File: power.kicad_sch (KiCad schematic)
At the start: 33 parts, among them U300 TPS563200, U301 TPS563200

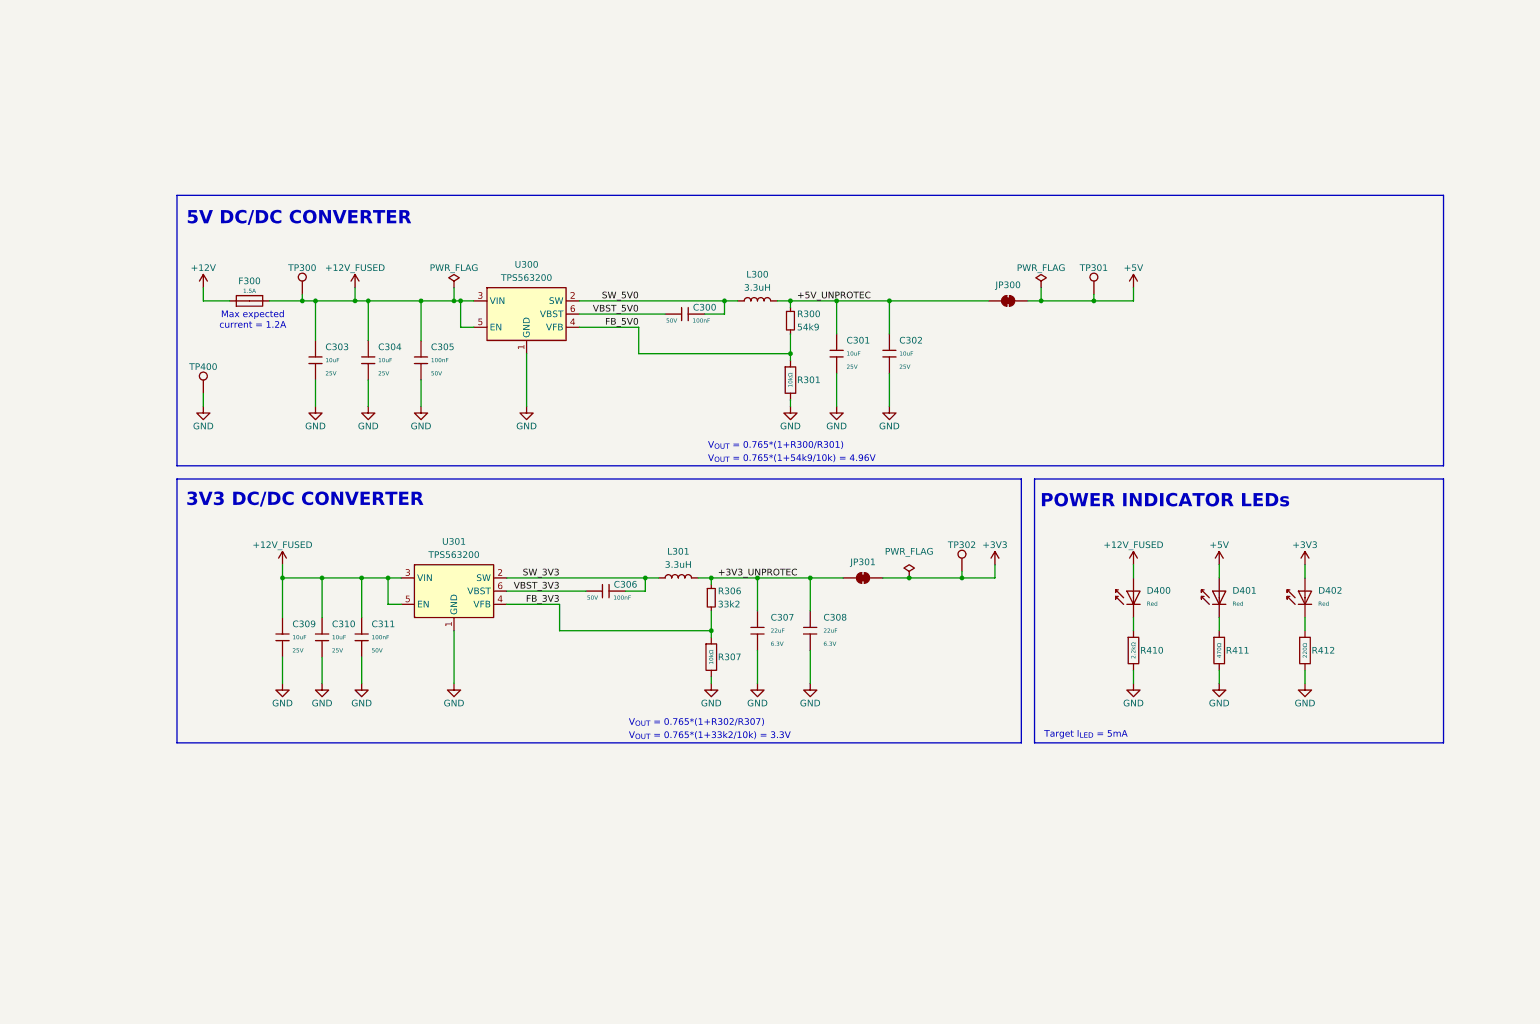
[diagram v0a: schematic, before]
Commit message: Add MX74700 lib and symbol
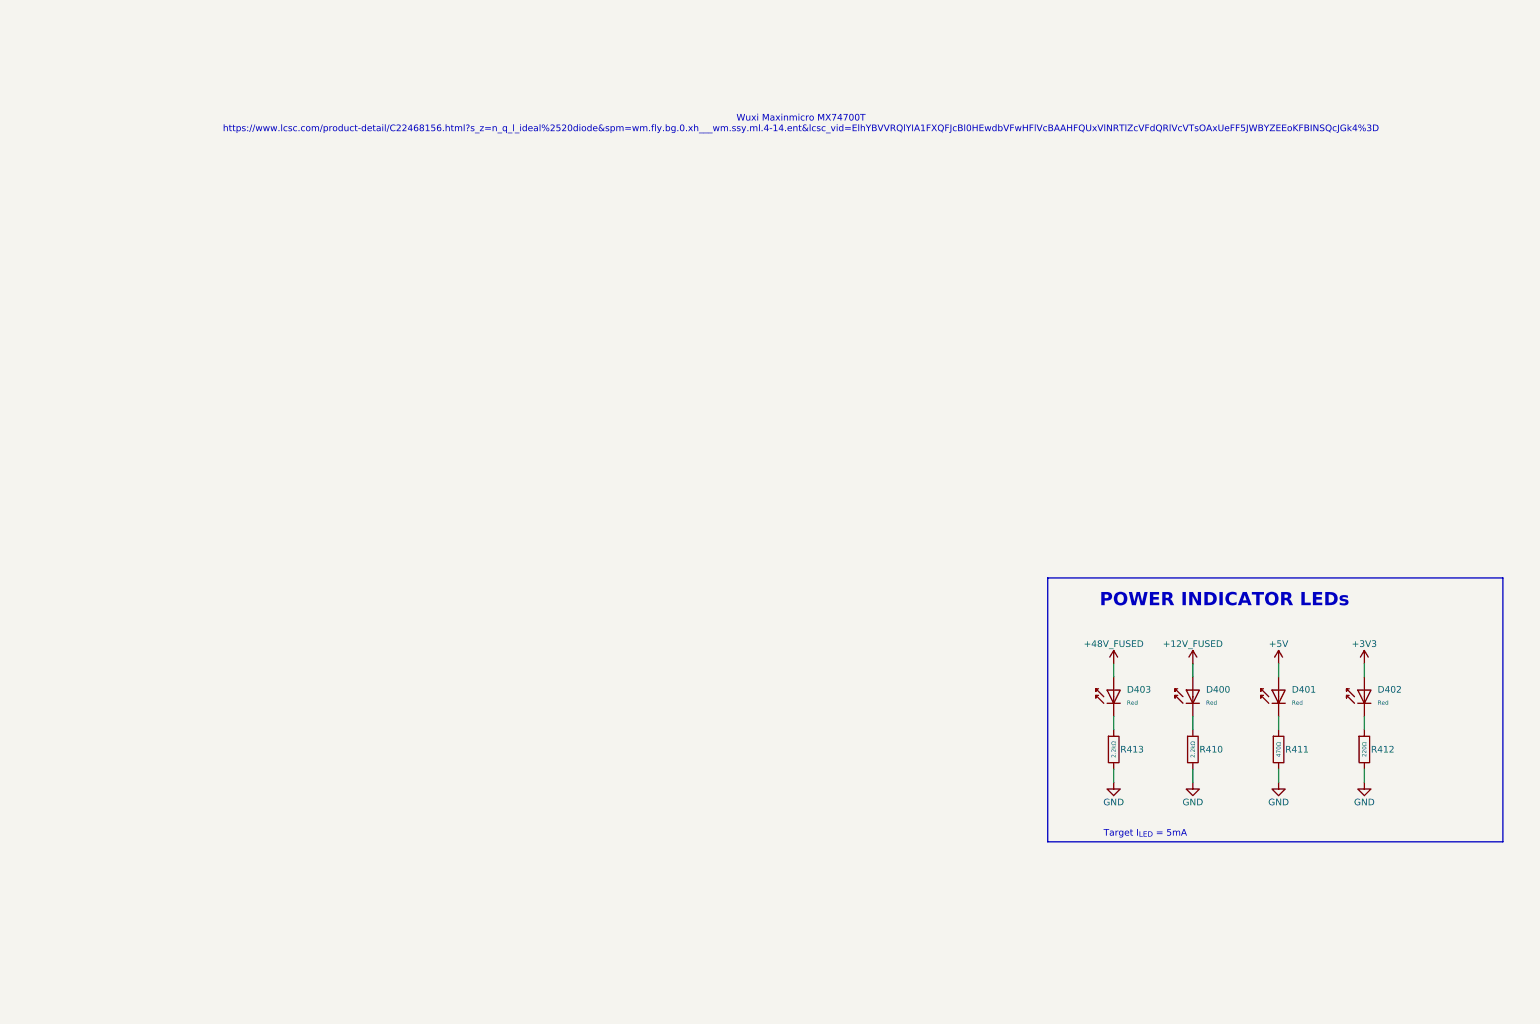
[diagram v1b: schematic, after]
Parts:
- removed C300, C305, C306, C311: 100nF, PCM_JLCPCB:C_0402, symbol PCM_JLCPCB-Capacitors:0402,100nF,(2)
- removed C301, C302, C303, C304, C309, C310: 10uF, PCM_JLCPCB:C_0603, symbol PCM_JLCPCB-Capacitors:0603,10uF,(2)
- removed C307, C308: 22uF, PCM_JLCPCB:C_0603, symbol PCM_JLCPCB-Capacitors:0603,22uF
- removed F300: 1.5A, PCM_JLCPCB:F_0603, symbol PCM_JLCPCB-Variable-Resistors:Fuse,1.5A
- removed JP300, JP301: SolderJumper_2_Bridged, Jumper:SolderJumper-2_P1.3mm_Open_TrianglePad1.0x1.5mm, symbol Jumper:SolderJumper_2_Bridged
- removed L300, L301: 3.3uH, Inductor_SMD:L_Changjiang_FXL0420, symbol Device:L
- removed R300: 54k9, PCM_JLCPCB:R_0402, symbol Device:R_Small
- removed R301, R307: 10kΩ, PCM_JLCPCB:R_0402, symbol PCM_JLCPCB-Resistors:0402,10kΩ
- removed R306: 33k2, PCM_JLCPCB:R_0402, symbol Device:R_Small
- removed TP300, TP301, TP302, TP400: TestPoint, TestPoint:TestPoint_Pad_D1.0mm, symbol Connector:TestPoint
- removed U300, U301: TPS563200, Package_TO_SOT_SMD:SOT-23-6, symbol Regulator_Switching:TPS563200
- added D403: Red, PCM_JLCPCB:D_0603, symbol PCM_JLCPCB-Diodes:LED,0603,Red
- added R413: 2.2kΩ, PCM_JLCPCB:R_0402, symbol PCM_JLCPCB-Resistors:0402,2.2kΩ
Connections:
- net GND: now also R413.2
- new net: D403.1, R413.1
- new net +48V_FUSED: D403.2
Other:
- note added: "Wuxi Maxinmicro MX74700T https://www.lcsc.com/product-detail/C22468156.html?s_z=n_q_l_ideal%2520diode&spm=wm.fly.bg.0.xh___wm.ssy.ml.4-14.ent&lcsc_vid=ElhYBVVRQlYIA1FXQFJcBl0HEwdbVFwHFlVcBAAHFQUxVlNRTlZcVFdQRlVcVTsOAxUeFF5JWBYZEEoKFBINSQcJGk4%3D"
- note removed: "3V3 DC/DC CONVERTER"
- note removed: "5V DC/DC CONVERTER"
- note removed: "Max expected current = 1.2A"
- note removed: "V_{OUT} = 0.765*(1+33k2/10k) = 3.3V"
- note removed: "V_{OUT} = 0.765*(1+54k9/10k) = 4.96V"
- note removed: "V_{OUT} = 0.765*(1+R300/R301)"
- note removed: "V_{OUT} = 0.765*(1+R302/R307)"
- title: ModuCard BM STM32H562VGT6 -> ModuCard 3 BM STM32H562VGT6
- moved on the sheet: D400, D401, D402, R410, R411, R412

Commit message: Write converter schematics
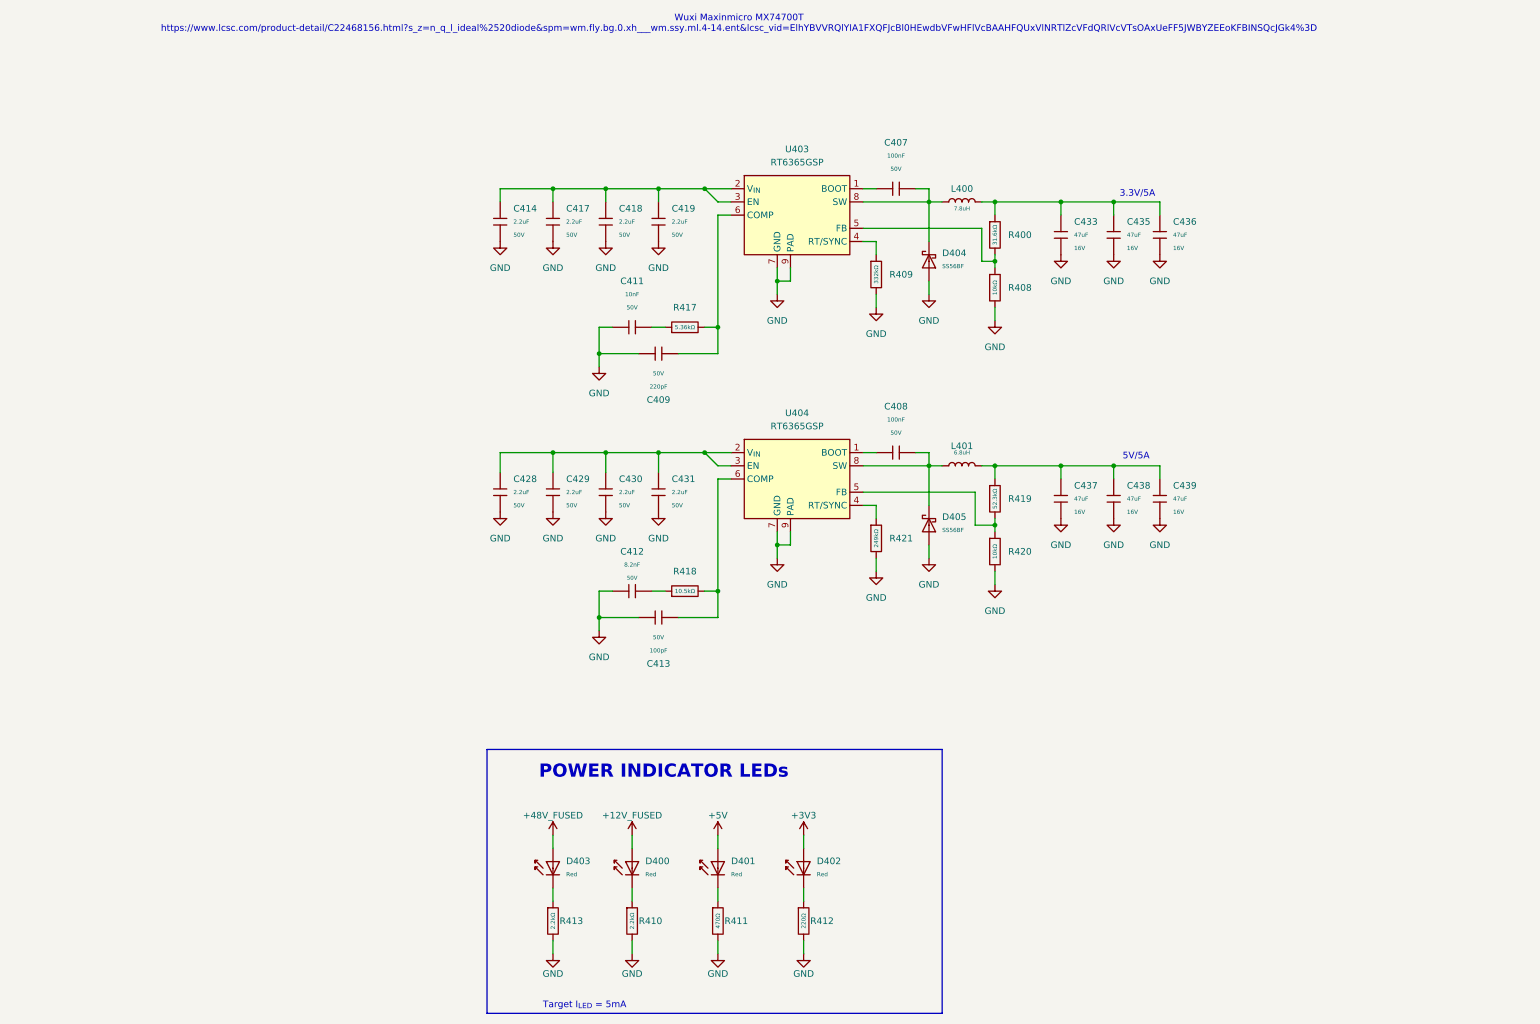
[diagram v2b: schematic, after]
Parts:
- added C407, C408: 100nF, PCM_JLCPCB:C_0603, symbol PCM_JLCPCB-Capacitors:0603,100nF
- added C409: 220pF, PCM_JLCPCB:C_0402, symbol PCM_JLCPCB-Capacitors:0402,220pF
- added C411: 10nF, PCM_JLCPCB:C_0402, symbol PCM_JLCPCB-Capacitors:0402,10nF
- added C412: 8.2nF, PCM_JLCPCB:C_0402, symbol PCM_JLCPCB-Capacitors:0402,10nF
- added C413: 100pF, PCM_JLCPCB:C_0402, symbol PCM_JLCPCB-Capacitors:0402,100pF
- added C414, C417, C418, C419, C428, C429, C430, C431: 2.2uF, PCM_JLCPCB:C_1206, symbol PCM_JLCPCB-Capacitors:1206,2.2uF
- added C433, C435, C436, C437, C438, C439: 47uF, Capacitor_SMD:C_1210_3225Metric, symbol PCM_JLCPCB-Capacitors:0603,100nF
- added D404, D405: SS56BF, PCM_JLCPCB:D_SMBF, symbol PCM_JLCPCB-Diodes:Schottky,SS56BF
- added L400: 7.8uH, Inductor_SMD:L_APV_APH1050, symbol FHC1050:FHC1050-7R8M
- added L401: 6.8uH, Inductor_SMD:L_Sunlord_MWSA0605S, symbol PSPMAA0605H:PSMAA0605H-6R8M-ANP
- added R400: 31.6kΩ, PCM_JLCPCB:R_0402, symbol PCM_JLCPCB-Resistors:0402,33kΩ
- added R408, R420: 10kΩ, PCM_JLCPCB:R_0402, symbol PCM_JLCPCB-Resistors:0402,10kΩ
- added R409: 332kΩ, PCM_JLCPCB:R_0402, symbol PCM_JLCPCB-Resistors:0402,0Ω
- added R417: 5.36kΩ, PCM_JLCPCB:R_0402, symbol PCM_JLCPCB-Resistors:0402,0Ω
- added R418: 10.5kΩ, PCM_JLCPCB:R_0402, symbol PCM_JLCPCB-Resistors:0402,0Ω
- added R419: 52.3kΩ, PCM_JLCPCB:R_0402, symbol PCM_JLCPCB-Resistors:0402,33kΩ
- added R421: 249kΩ, PCM_JLCPCB:R_0402, symbol PCM_JLCPCB-Resistors:0402,0Ω
- added U403, U404: RT6365GSP, Package_SO:SOIC-8-1EP_3.9x4.9mm_P1.27mm_EP2.29x3mm, symbol RT6365:RT6365GSP
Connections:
- net GND: now also C409.1, C411.1, C412.1, C413.1, C414.2, C417.2, C418.2, C419.2, C428.2, C429.2, C430.2, C431.2, C433.2, C435.2, C436.2, C437.2, C438.2, C439.2, D404.2, D405.2, R408.2, R409.2, R420.2, R421.2, U403.7 (GND), U403.9 (PAD), U404.7 (GND), U404.9 (PAD)
- new net: C414.1, C417.1, C418.1, C419.1, U403.2 (V_{IN}), U403.3 (EN)
- new net: R400.2, R408.1, U403.5 (FB)
- new net: C407.2, D404.1, L400.1, U403.8 (SW)
- new net: C408.2, D405.1, L401.1, U404.8 (SW)
- new net: C437.1, C438.1, C439.1, L401.2, R419.1
- new net: C433.1, C435.1, C436.1, L400.2, R400.1
- new net: C407.1, U403.1 (BOOT)
- new net: R409.1, U403.4 (RT/SYNC)
- new net: C409.2, R417.2, U403.6 (COMP)
- new net: C428.1, C429.1, C430.1, C431.1, U404.2 (V_{IN}), U404.3 (EN)
- new net: R419.2, R420.1, U404.5 (FB)
- new net: R421.1, U404.4 (RT/SYNC)
- new net: C408.1, U404.1 (BOOT)
- new net: C411.2, R417.1
- new net: C412.2, R418.1
- new net: C413.2, R418.2, U404.6 (COMP)
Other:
- note added: "3.3V/5A"
- note added: "5V/5A"
- moved on the sheet: D400, D401, D402, D403, R410, R411, R412, R413
